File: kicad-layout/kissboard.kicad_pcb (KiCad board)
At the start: 2 copper layers, 131.1 x 102.7 mm, 27 parts, among them J1 Conn_01x04, K1 KEYSW, K10 KEYSW, K11 KEYSW, K12 KEYSW, K13 KEYSW, K14 KEYSW, K15 KEYSW, K16 KEYSW, K17 KEYSW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

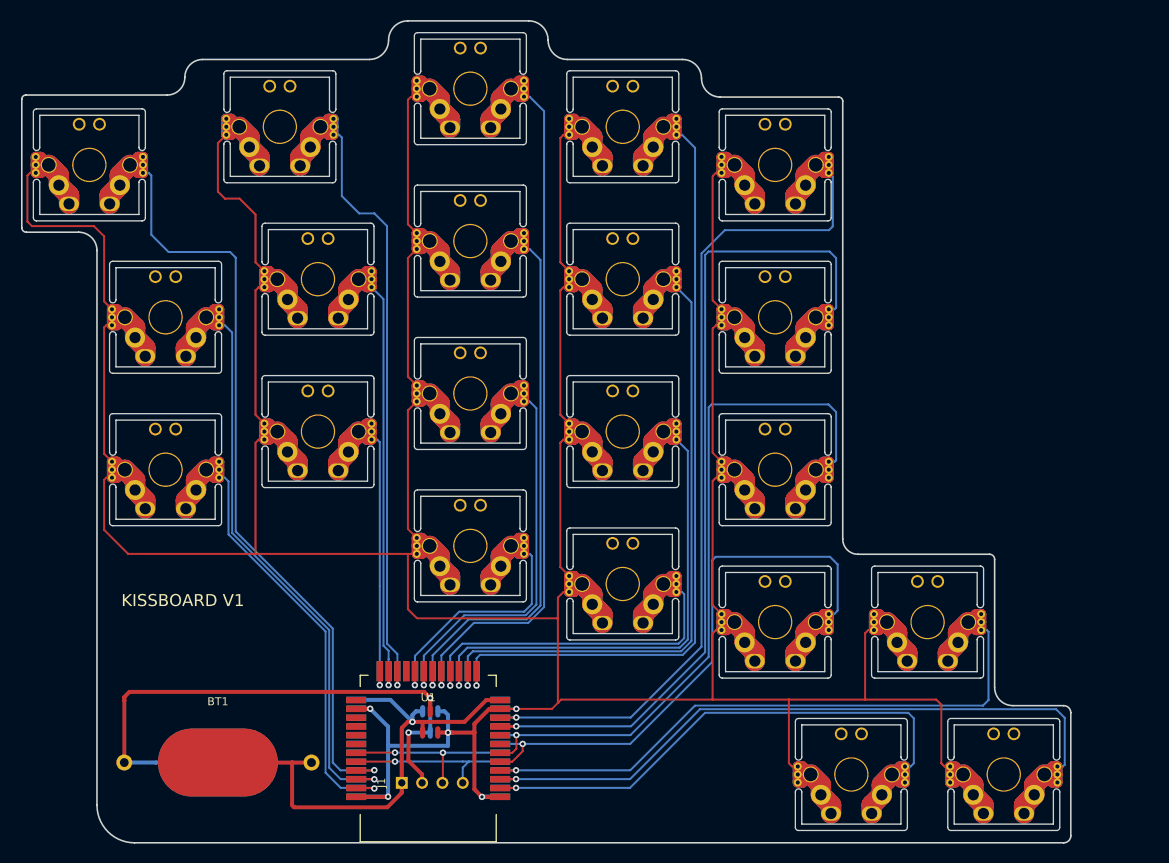
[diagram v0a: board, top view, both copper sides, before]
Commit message: Reshaping of PCB. Cleaning of old tracks in the works...
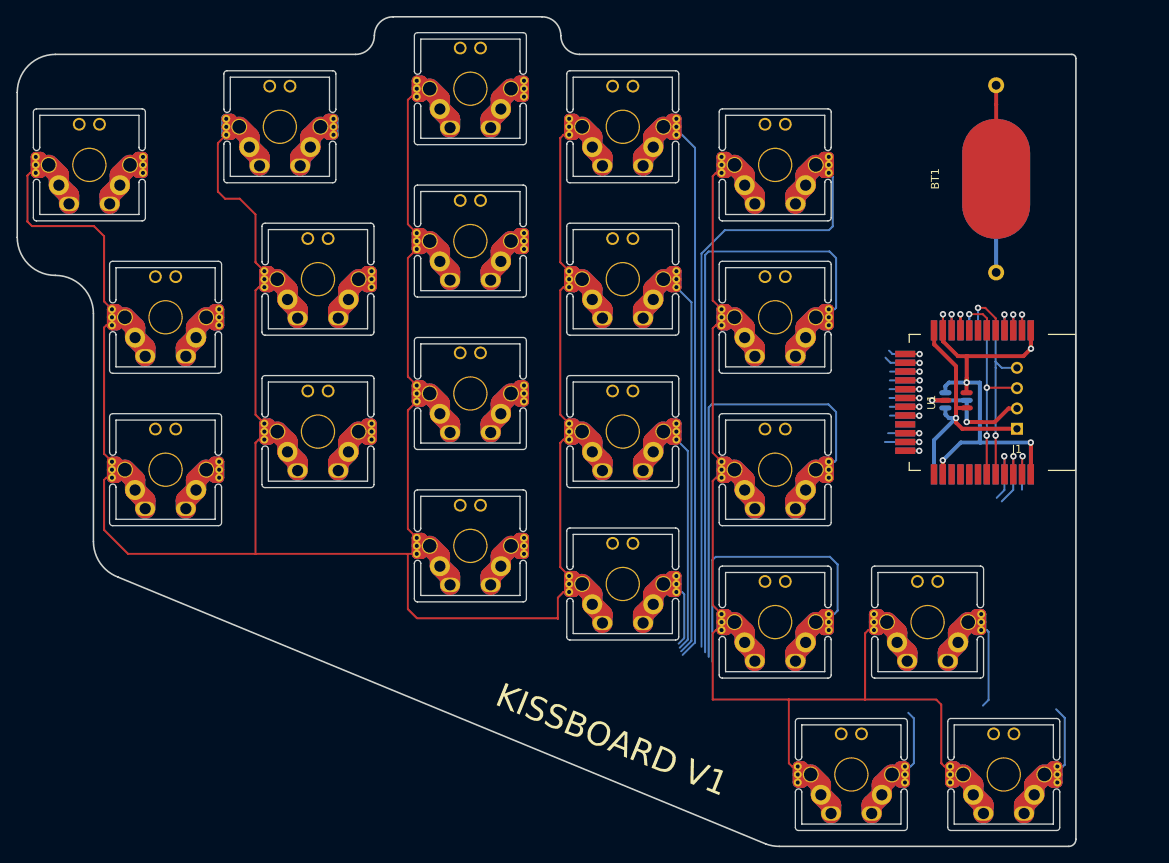
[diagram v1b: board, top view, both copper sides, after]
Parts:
- moved BT1 121.6 mm to (156.2, 42.2), turned to 270 degrees
- moved J1 88.7 mm to (158.8, 73.5), turned to 0 degrees
- moved U1 83.4 mm to (155.7, 70.2), turned to 270 degrees
- moved U2 83.4 mm to (155.7, 70.2), turned to 90 degrees
- moved Q1 77.0 mm to (151.2, 69.9), turned to 180 degrees
- moved Q2 77.0 mm to (151.2, 69.9), turned to 0 degrees
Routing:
- net /S1: track 123.6 -> 35.1 mm
- net /S3: track 115.3 -> 34.7 mm
- net /S21: track 110.7 -> 39.6 mm
- net /S2: track 100.6 -> 30.9 mm
- net /S8: track 94.6 -> 32.7 mm
- net /S19: track 103.4 -> 41.7 mm
- net /S6: track 97.2 -> 35.8 mm
- net /S20: track 92.0 -> 39.1 mm
- net /GND_BAT: track 74.4 -> 27.4 mm
- net /S7: track 79.6 -> 33.3 mm
- net /S11: track 79.2 -> 33.7 mm
- net /S13: track 76.0 -> 32.8 mm
- net GND: track 1077.2 -> 1041.7 mm
- net /S12: track 60.5 -> 30.7 mm
- net /S17: track 69.5 -> 40.3 mm
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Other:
- board size 131.1 x 102.7 mm -> 132.3 x 103.7 mm

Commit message: Completed cleaning of tracks for new placement and added updated pictures.
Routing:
- net /S5: track 105.1 -> 31.3 mm
- net /S10: track 107.0 -> 33.3 mm
- net /S4: track 100.1 -> 30.8 mm
- net /S15: track 89.9 -> 35.2 mm
- net GND: track 1041.7 -> 1093.3 mm
- net /S9: track 80.4 -> 30.8 mm
- net /S18: track 73.1 -> 37.8 mm
- net /S14: track 59.7 -> 30.8 mm
- net /S19: track 41.7 -> 31.2 mm
- net /S17: track 40.3 -> 30.8 mm
- net /S21: track 39.6 -> 31.2 mm
- net /S20: track 39.1 -> 31.2 mm
- net /S6: track 35.8 -> 31.8 mm
- net /S1: track 35.1 -> 31.8 mm
- net /S7: track 33.3 -> 30.7 mm
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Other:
- outline, holes or cut-outs redrawn

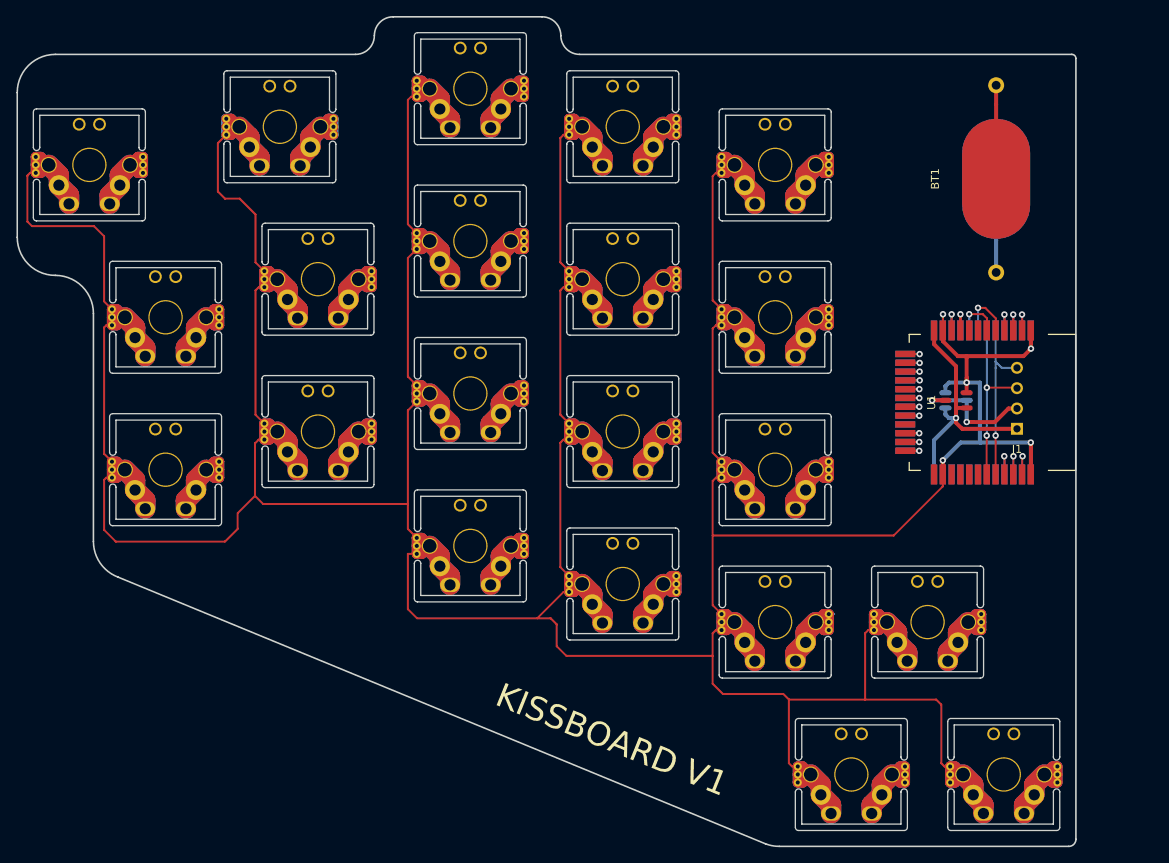
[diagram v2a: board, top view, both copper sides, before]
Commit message: traces complete, all files updated, gerber.zip added
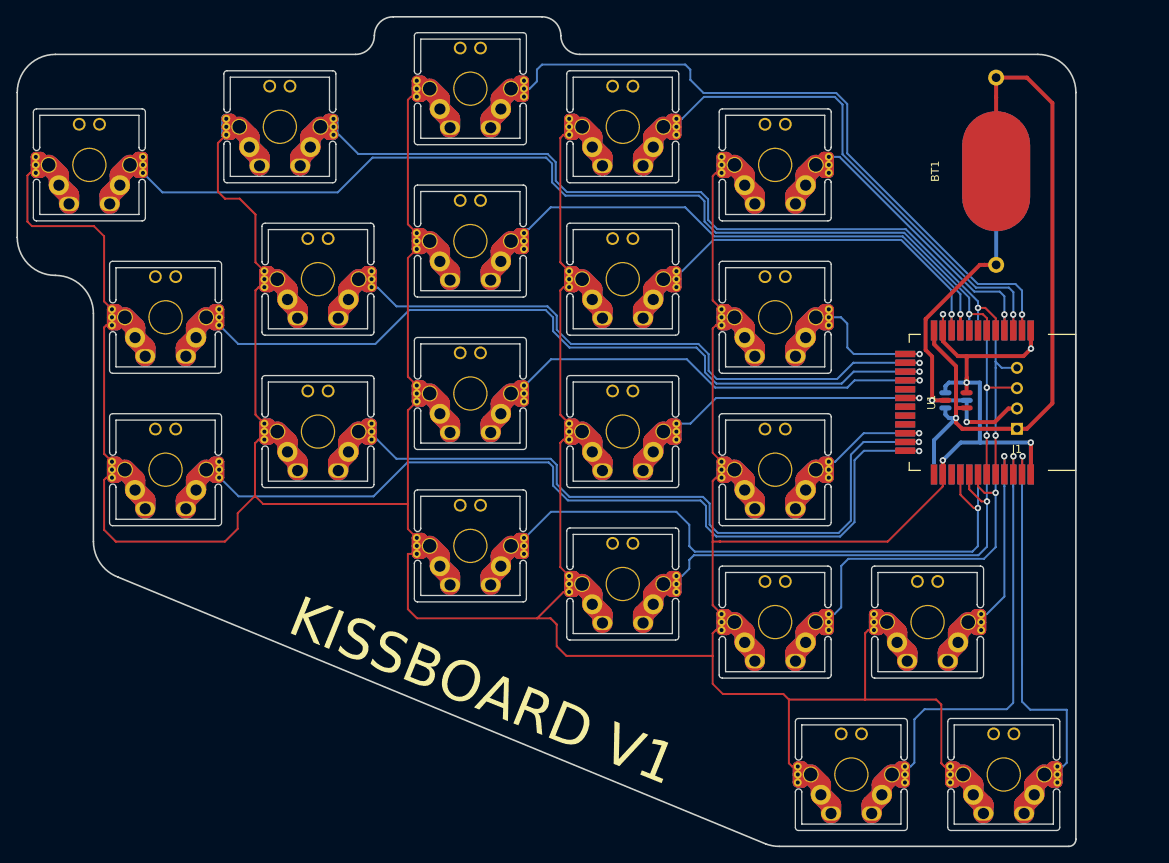
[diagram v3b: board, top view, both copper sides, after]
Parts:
- moved BT1 0.95 mm to (156.2, 41.3)
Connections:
- U1 pad 10: /S5 -> /S9
- U1 pad 13: /S4 -> /S10
- U1 pad 14: /S9 -> /S7
- U1 pad 15: /S14 -> /S6
- U1 pad 16: /S17 -> /S13
- U1 pad 17: /S3 -> Net-(U1-Pad17)
- U1 pad 18: /S8 -> /S14
- U1 pad 19: /S13 -> Net-(U1-Pad19)
- U1 pad 2: /S20 -> /S3
- U1 pad 20: /S16 -> Net-(U1-Pad20)
- U1 pad 22: /S2 -> /S15
- U1 pad 23: /S7 -> /S12
- U1 pad 24: /S12 -> /S11
- U1 pad 28: Net-(U1-Pad28) -> /S16
- U1 pad 29: Net-(U1-Pad29) -> /S17
- U1 pad 3: /S21 -> /S4
- U1 pad 30: Net-(U1-Pad30) -> /S18
- U1 pad 33: /S1 -> /S19
- U1 pad 34: /S6 -> /S20
- U1 pad 35: /S11 -> /S21
- U1 pad 4: /S19 -> /S5
- U1 pad 5: /S18 -> /S2
- U1 pad 6: /S15 -> /S1
- U1 pad 9: /S10 -> /S8
- U2 pad 13: /S12 -> /S11
- U2 pad 14: /S7 -> /S12
- U2 pad 15: /S2 -> /S15
- U2 pad 17: /S16 -> Net-(U2-Pad17)
- U2 pad 18: /S13 -> Net-(U2-Pad18)
- U2 pad 19: /S8 -> /S14
- U2 pad 2: /S11 -> /S21
- U2 pad 20: /S3 -> Net-(U2-Pad20)
- U2 pad 21: /S17 -> /S13
- U2 pad 22: /S14 -> /S6
- U2 pad 23: /S9 -> /S7
- U2 pad 24: /S4 -> /S10
- U2 pad 27: /S5 -> /S9
- U2 pad 28: /S10 -> /S8
- U2 pad 29: /S15 -> /S1
- U2 pad 3: /S6 -> /S20
- U2 pad 30: /S18 -> /S2
- U2 pad 33: /S19 -> /S5
- U2 pad 34: /S21 -> /S4
- U2 pad 35: /S20 -> /S3
- U2 pad 4: /S1 -> /S19
- U2 pad 5: Net-(U2-Pad5) -> /S18
- U2 pad 6: Net-(U2-Pad6) -> /S17
- U2 pad 7: Net-(U2-Pad7) -> /S16
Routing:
- net /S1: track 31.8 -> 153.5 mm
- net /S11: track 31.8 -> 134.9 mm
- net /S2: track 28.7 -> 128.0 mm
- net /S6: track 31.8 -> 125.9 mm
- net /S12: track 30.7 -> 114.7 mm
- net /S3: track 32.8 -> 116.7 mm
- net /S7: track 30.7 -> 105.4 mm
- net /S16: track 32.8 -> 105.7 mm
- net /S8: track 30.8 -> 96.2 mm
- net /S4: track 30.8 -> 91.0 mm
- net VCC: track 44.3 -> 95.9 mm
- net /S17: track 30.8 -> 82.0 mm
- net /S13: track 30.9 -> 81.9 mm
- net /S20: track 31.2 -> 80.3 mm
- net /S21: track 31.2 -> 74.9 mm
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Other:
- outline, holes or cut-outs redrawn

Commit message: Fixed wrong connection of S16 on the bottom layer
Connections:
- U2 pad 7: /S16 -> Net-(U2-Pad7)
- U2 pad 9: Net-(U2-Pad9) -> /S16
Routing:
- net /S16: track 105.7 -> 101.3 mm
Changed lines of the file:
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@@
     (thickness 1.6)
     (drawings 21)
-    (tracks 1366)
+    (tracks 1365)
     (zones 0)
     (modules 27)
@@
   (net 34 "Net-(U1-Pad21)")
   (net 35 "Net-(U1-Pad27)")
-  (net 36 "Net-(U2-Pad9)")
-  (net 37 "Net-(U2-Pad17)")
-  (net 38 "Net-(U2-Pad18)")
-  (net 39 "Net-(U2-Pad20)")
-  (net 40 "Net-(U1-Pad17)")
-  (net 41 "Net-(U1-Pad19)")
-  (net 42 "Net-(U1-Pad20)")
+  (net 36 "Net-(U2-Pad17)")
+  (net 37 "Net-(U2-Pad18)")
+  (net 38 "Net-(U2-Pad20)")
+  (net 39 "Net-(U1-Pad17)")
+  (net 40 "Net-(U1-Pad19)")
+  (net 41 "Net-(U1-Pad20)")
+  (net 42 "Net-(U2-Pad7)")
   (net_class Default "This is the default net class."
     (clearance 0.2)
@@
     (add_net "Net-(U2-Pad20)")
     (add_net "Net-(U2-Pad25)")
+    (add_net "Net-(U2-Pad7)")
     (add_net "Net-(U2-Pad8)")
-    (add_net "Net-(U2-Pad9)")
     (add_net VCC)
   )
@@
       (net 8 /S13))
     (pad 17 smd rect (at -1.65 10.9 270) (size 0.8 2.5) (layers F.Cu F.Paste F.Mask)
-      (net 40 "Net-(U1-Pad17)"))
+      (net 39 "Net-(U1-Pad17)"))
     (pad 18 smd rect (at -0.55 10.9 270) (size 0.8 2.5) (layers F.Cu F.Paste F.Mask)
       (net 5 /S14))
     (pad 19 smd rect (at 0.55 10.9 270) (size 0.8 2.5) (layers F.Cu F.Paste F.Mask)
-      (net 41 "Net-(U1-Pad19)"))
+      (net 40 "Net-(U1-Pad19)"))
     (pad 20 smd rect (at 1.65 10.9 270) (size 0.8 2.5) (layers F.Cu F.Paste F.Mask)
-      (net 42 "Net-(U1-Pad20)"))
+      (net 41 "Net-(U1-Pad20)"))
     (pad 21 smd rect (at 2.75 10.9 270) (size 0.8 2.5) (layers F.Cu F.Paste F.Mask)
       (net 34 "Net-(U1-Pad21)"))
@@
       (net 32 "Net-(U2-Pad16)"))
     (pad 17 smd rect (at -1.65 -10.9 90) (size 0.8 2.5) (layers B.Cu B.Paste B.Mask)
-      (net 37 "Net-(U2-Pad17)"))
+      (net 36 "Net-(U2-Pad17)"))
     (pad 18 smd rect (at -0.55 -10.9 90) (size 0.8 2.5) (layers B.Cu B.Paste B.Mask)
-      (net 38 "Net-(U2-Pad18)"))
+      (net 37 "Net-(U2-Pad18)"))
     (pad 19 smd rect (at 0.55 -10.9 90) (size 0.8 2.5) (layers B.Cu B.Paste B.Mask)
       (net 5 /S14))
     (pad 20 smd rect (at 1.65 -10.9 90) (size 0.8 2.5) (layers B.Cu B.Paste B.Mask)
-      (net 39 "Net-(U2-Pad20)"))
+      (net 38 "Net-(U2-Pad20)"))
     (pad 21 smd rect (at 2.75 -10.9 90) (size 0.8 2.5) (layers B.Cu B.Paste B.Mask)
       (net 8 /S13))
@@
       (net 24 /S17))
     (pad 7 smd rect (at -9 -1.8) (size 0.8 2.5) (layers B.Cu B.Paste B.Mask)
-      (net 27 /S16))
+      (net 42 "Net-(U2-Pad7)"))
     (pad 8 smd rect (at -9 -2.9) (size 0.8 2.5) (layers B.Cu B.Paste B.Mask)
       (net 19 "Net-(U2-Pad8)"))
     (pad 9 smd rect (at -9 -4) (size 0.8 2.5) (layers B.Cu B.Paste B.Mask)
-      (net 36 "Net-(U2-Pad9)"))
+      (net 27 /S16))
     (pad 10 smd rect (at -9 -5.1) (size 0.8 2.5) (layers B.Cu B.Paste B.Mask)
       (net 33 "Net-(U2-Pad10)"))
@@
   (segment (start 151.1935 70.8025) (end 151.1935 66.294) (width 0.5) (layer F.Cu) (net 22))
   (segment (start 151.1935 66.294) (end 151.1935 65.6455) (width 0.5) (layer F.Cu) (net 22))
+  (segment (start 151.765 77.2795) (end 151.765 79.147) (width 0.25) (layer F.Cu) (net 27))
+  (segment (start 151.765 79.147) (end 151.7435 79.1685) (width 0.25) (layer F.Cu) (net 27))
+  (segment (start 151.7435 77.301) (end 151.765 77.2795) (width 0.25) (layer B.Cu) (net 27))
+  (segment (start 151.7435 79.1685) (end 151.7435 77.301) (width 0.25) (layer B.Cu) (net 27))
+  (via (at 151.765 77.2795) (size 0.8) (drill 0.4) (layers F.Cu B.Cu) (net 27))
+  (segment (start 150.12502 88.82548) (end 151.7435 87.207) (width 0.25) (layer B.Cu) (net 27))
+  (segment (start 151.7435 87.207) (end 151.7435 79.1685) (width 0.25) (layer B.Cu) (net 27))
+  (segment (start 118.54348 88.82548) (end 150.12502 88.82548) (width 0.25) (layer B.Cu) (net 27))
   (segment (start 117.856 88.138) (end 118.54348 88.82548) (width 0.25) (layer B.Cu) (net 27))
   (segment (start 117.856 85.471) (end 117.856 88.138) (width 0.25) (layer B.Cu) (net 27))
@@
   (segment (start 97.1875 87.10625) (end 97.29775 87.10625) (width 0.25) (layer B.Cu) (net 27))
   (segment (start 97.29775 87.10625) (end 100.5586 83.8454) (width 0.25) (layer B.Cu) (net 27))
-  (segment (start 118.54348 88.82548) (end 153.23652 88.82548) (width 0.25) (layer B.Cu) (net 27))
-  (segment (start 153.23652 88.82548) (end 153.924 88.138) (width 0.25) (layer B.Cu) (net 27))
-  (segment (start 153.924 88.138) (end 153.924 83.3755) (width 0.25) (layer B.Cu) (net 27))
   (segment (start 156.21 52.975) (end 156.21 41.275) (width 0.5) (layer B.Cu) (net 30))
   (segment (start 148.209001 64.436559) (end 147.3962 63.623758) (width 0.5) (layer F.Cu) (net 30))
@@
   (segment (start 154.176998 52.975) (end 154.795787 52.975) (width 0.5) (layer F.Cu) (net 30))
   (segment (start 154.795787 52.975) (end 156.21 52.975) (width 0.5) (layer F.Cu) (net 30))
-  (segment (start 144.86904 68.51396) (end 144.8655 68.5175) (width 0.25) (layer F.Cu) (net 40))
+  (segment (start 144.86904 68.51396) (end 144.8655 68.5175) (width 0.25) (layer F.Cu) (net 39))
   (segment (start 97.1875 31.95625) (end 96.5675 31.95625) (width 1.27) (layer F.Cu) (net 4))
   (segment (start 96.5675 31.95625) (end 95.5675 30.95625) (width 1.27) (layer F.Cu) (net 4))
@@
   (segment (start 94.2975 52.54625) (end 94.2975 51.27625) (width 2.54) (layer F.Cu) (net 7))
   (segment (start 94.2975 51.27625) (end 95.5675 50.00625) (width 2.54) (layer F.Cu) (net 7))
-  (segment (start 144.868496 70.714504) (end 144.8655 70.7175) (width 0.25) (layer F.Cu) (net 41))
+  (segment (start 144.868496 70.714504) (end 144.8655 70.7175) (width 0.25) (layer F.Cu) (net 40))
   (segment (start 97.1875 70.05625) (end 96.5675 70.05625) (width 1.27) (layer F.Cu) (net 8))
   (segment (start 96.5675 70.05625) (end 95.5675 69.05625) (width 1.27) (layer F.Cu) (net 8))
@@
   (segment (start 56.1975 62.07125) (end 56.1975 60.80125) (width 2.54) (layer F.Cu) (net 13))
   (segment (start 56.1975 60.80125) (end 57.4675 59.53125) (width 2.54) (layer F.Cu) (net 13))
-  (segment (start 153.416 83.3755) (end 151.7435 81.703) (width 0.25) (layer F.Cu) (net 27))
-  (segment (start 153.924 83.3755) (end 153.416 83.3755) (width 0.25) (layer F.Cu) (net 27))
-  (segment (start 151.7435 81.703) (end 151.7435 79.1685) (width 0.25) (layer F.Cu) (net 27))
-  (segment (start 153.9435 83.356) (end 153.924 83.3755) (width 0.25) (layer B.Cu) (net 27))
-  (segment (start 153.9435 79.1685) (end 153.9435 83.356) (width 0.25) (layer B.Cu) (net 27))
-  (via (at 153.924 83.3755) (size 0.8) (drill 0.4) (layers F.Cu B.Cu) (net 27))
   (segment (start 159.4435 102.2985) (end 159.4435 79.1685) (width 0.25) (layer B.Cu) (net 31))
   (segment (start 159.4435 102.992) (end 159.4435 102.2985) (width 0.25) (layer B.Cu) (net 31))
@@
   (segment (start 140.6525 121.55805) (end 140.6525 120.49125) (width 2.54) (layer B.Cu) (net 26))
   (segment (start 140.6525 120.49125) (end 141.9225 119.22125) (width 2.54) (layer B.Cu) (net 26))
-  (segment (start 144.88174 71.83374) (end 144.8655 71.8175) (width 0.25) (layer F.Cu) (net 42))
+  (segment (start 144.88174 71.83374) (end 144.8655 71.8175) (width 0.25) (layer F.Cu) (net 41))
   (segment (start 97.1875 89.10625) (end 96.5675 89.10625) (width 1.27) (layer B.Cu) (net 27))
   (segment (start 96.5675 89.10625) (end 95.5675 88.10625) (width 1.27) (layer B.Cu) (net 27))
